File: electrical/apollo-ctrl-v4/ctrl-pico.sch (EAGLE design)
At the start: 30 parts, among them J1 ESP32-PICO-KIT, J2 DNP, J3 DNP, U1 24LC01BT-I/SN

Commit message: Update valve board schematic
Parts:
- added C5, C7: 1u, apollo-ctrl-v4:CAP0805
- added C6: 0.1u, apollo-ctrl-v4:CAP0805
- added C8: 47uF, SparkFun-Capacitors:47UF-POLAR-PANASONIC_D-35V-20%
- added J4: (no value), SparkFun-Connectors:CONN_02
- added J5: M5PWR, SparkFun-Connectors:USB_A_SMT_FEMALE
- added J6: DNP, SparkFun-Connectors:CONN_03
- added JP1, JP2, JP3: M5PWR, SparkFun-Jumpers:JUMPER-SMT_2_NO_NO-SILK
- added R20, R21: 100, apollo-ctrl-v4:RESISTOR0805-RES
- added U2: M5STACK, apollo-ctrl-v4:M5STACK
- C4: value 0.1u -> DNP
- R2, R3, R4: value 10K -> DNP
- U1: value 24LC01BT-I/SN -> DNP (24LC01)
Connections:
- removed net GPIO18: J1.IO18, U$1.PIN15
- removed net GPIO19: J1.IO19, U$1.PIN42
- removed net GPIO21: J1.IO21, U$1.PIN18
- new net !IRQ!: J1.IO21, U$1.PIN16
- new net M33V: C5.1, C6.1, U2.3V3
- new net M5V: JP1.2, U2.5V
- new net MRX: R21.2, U2.G3-RXD1
- new net MRX2: J6.1, U2.G13-RXD2
- new net MSCL: JP2.2, U2.G33-SCL
- new net MSDA: JP3.2, U2.G32-SDA
- new net MTX: R20.2, U2.G1-TXD1
- new net MTX2: J6.3, U2.G14-TXD2
- new net SCL2: J1.IO19
- new net SDA2: J1.IO18
- net +5V: now also C7.1, C8.+, J4.2, J5.VBUS, JP1.1
- net GND: now also C5.2, C6.2, C7.2, C8.-, J4.1, J5.GND, J5.SHLD, J6.2, U2.GND
- net GPIO22: now also R20.1, U$1.PIN15; no longer U$1.PIN17
- net GPIO23: now also R21.1, U$1.PIN42; no longer U$1.PIN16
- net SCL: now also JP2.1
- net SDA: now also JP3.1
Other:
- note added: "DigiKey: WM6294CT-ND"
- note added: "M5 hole: 3.1mm, 44mm C2C Pads 4.6mm (rows) 2.54mm (cols), 1.66mm x 2.6mm"
- note added: "NO PERIPHERAL USE For I2C on board M5Stack"

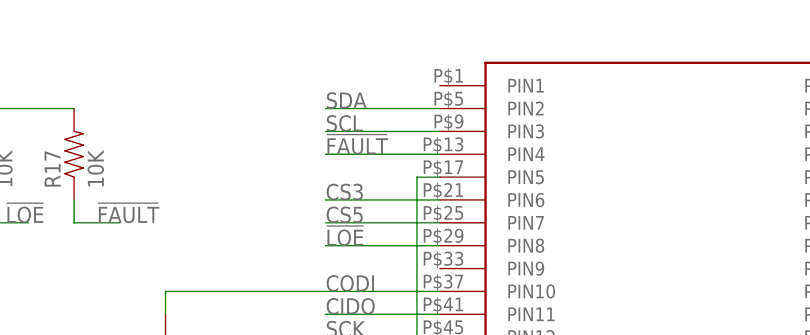
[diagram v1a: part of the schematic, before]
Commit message: Add stepper drivers to the valve board schematic. No guarantee that they fit, but if they do not another board can be made.
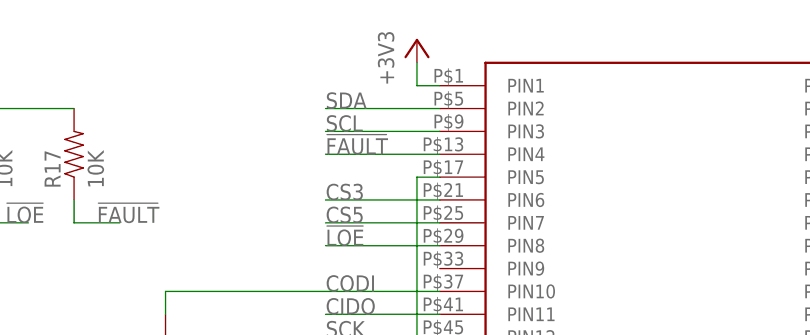
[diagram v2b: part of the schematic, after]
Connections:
- net +3V3: now also U$1.PIN1
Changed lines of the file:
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@@
 <part name="J6" library="SparkFun-Connectors" deviceset="CONN_03" device="" value="DNP"/>
 <part name="GND16" library="supply1" deviceset="GND" device=""/>
+<part name="+3V5" library="supply1" deviceset="+3V3" device=""/>
 </parts>
 <sheets>
@@
 <instance part="GND16" gate="1" x="289.56" y="96.52" smashed="yes">
 <attribute name="VALUE" x="287.02" y="93.98" size="1.778" layer="96"/>
+</instance>
+<instance part="+3V5" gate="G$1" x="104.14" y="182.88" smashed="yes">
+<attribute name="VALUE" x="101.6" y="177.8" size="1.778" layer="96" rot="R90"/>
 </instance>
 </instances>
@@
 <junction x="55.88" y="175.26"/>
 </segment>
-</net>
+<segment>
+<pinref part="+3V5" gate="G$1" pin="+3V3"/>
+<wire x1="104.14" y1="180.34" x2="104.14" y2="177.8" width="0.1524" layer="91"/>
+<pinref part="U$1" gate="G$1" pin="PIN1"/>
+<wire x1="104.14" y1="177.8" x2="106.68" y2="177.8" width="0.1524" layer="91"/>
+</segment>
+</net>

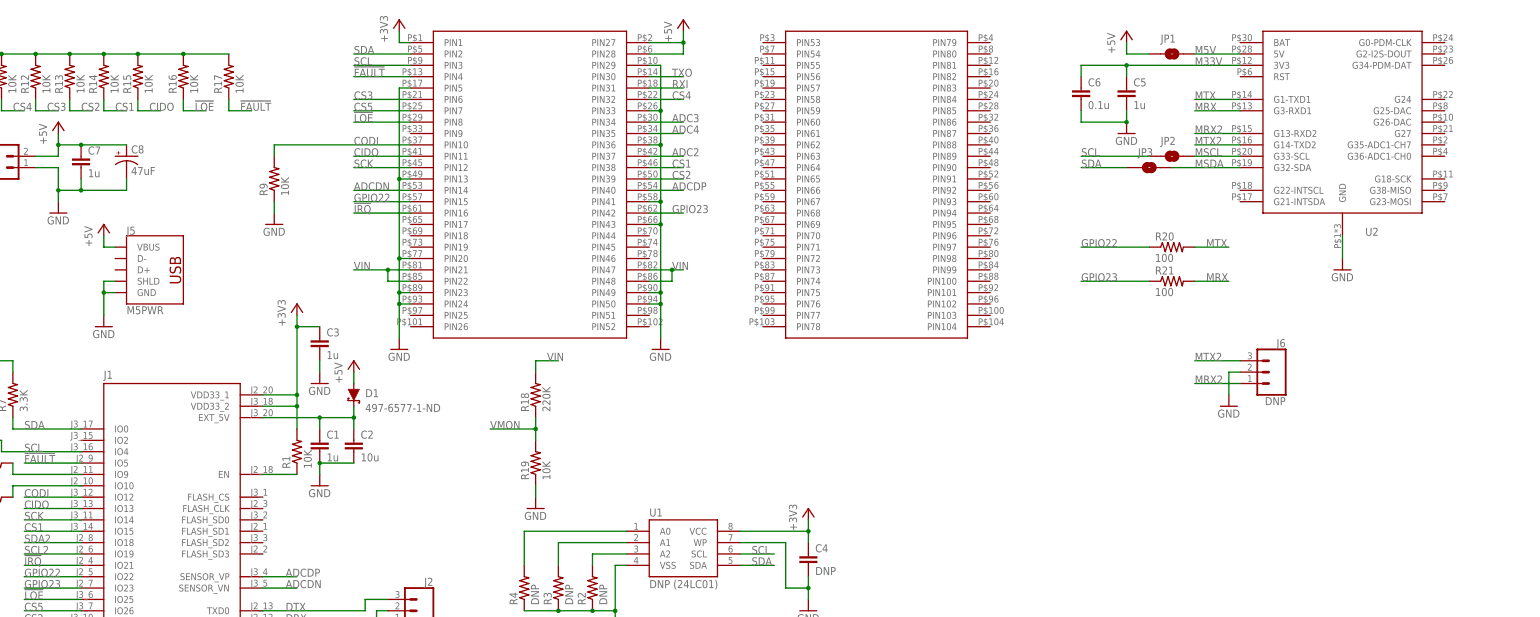
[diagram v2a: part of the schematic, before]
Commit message: Switch Apollo control board to use discrete SPI LCD and no M5-Stack
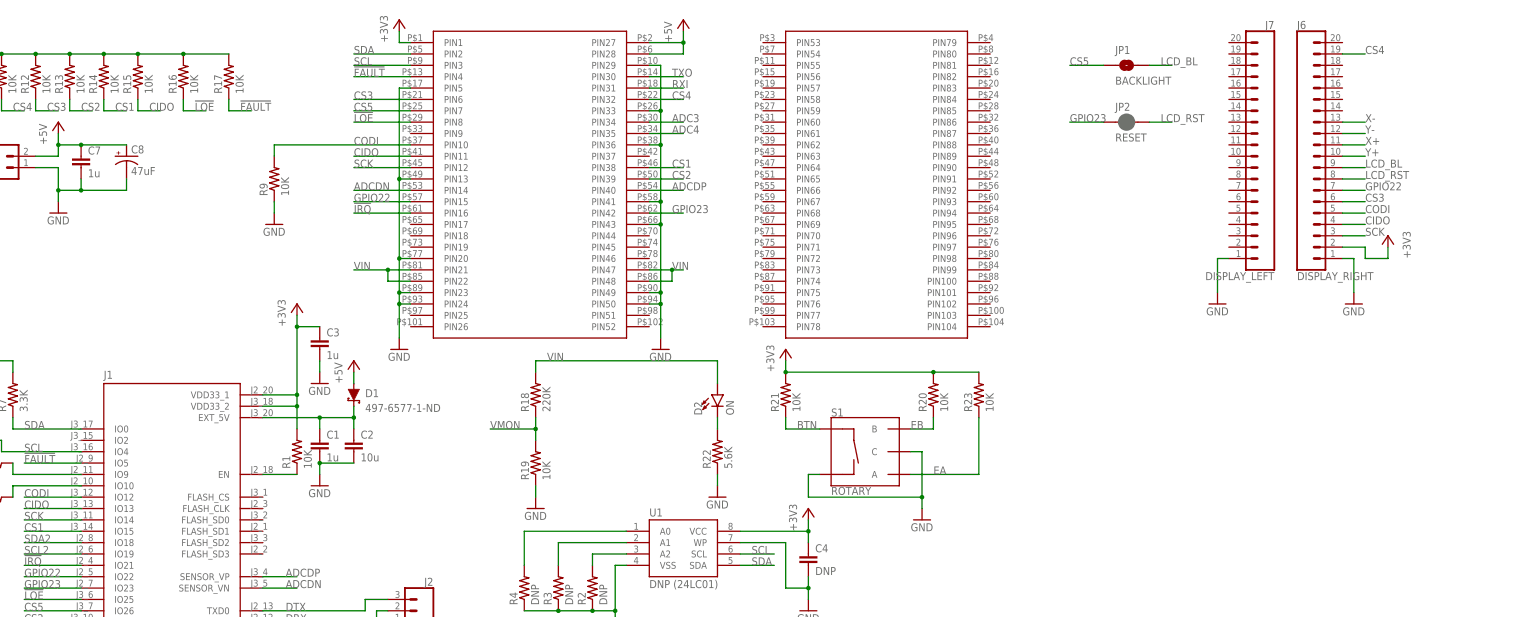
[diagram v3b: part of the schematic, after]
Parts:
- removed C5: 1u, apollo-ctrl-v4:CAP0805
- removed C6: 0.1u, apollo-ctrl-v4:CAP0805
- removed J5: M5PWR, SparkFun-Connectors:USB_A_SMT_FEMALE
- removed JP3: M5PWR, SparkFun-Jumpers:JUMPER-SMT_2_NO_NO-SILK
- removed U2: M5STACK, apollo-ctrl-v4:M5STACK
- added D2: ON, SparkFun-LED:LED-GREEN0603
- added J7: DISPLAY_LEFT, SparkFun-Connectors:CONN_20
- added R22: 5.6K, apollo-ctrl-v4:RESISTOR0805-RES
- added R23: 10K, apollo-ctrl-v4:RESISTOR0805-RES
- added S1: ROTARY, SparkFun-Switches:ENCODER-SWITCH
- J6: value DNP -> DISPLAY_RIGHT; device SparkFun-Connectors:CONN_03 -> SparkFun-Connectors:CONN_20
- JP1: value M5PWR -> BACKLIGHT
- JP2: value M5PWR -> RESET; device SparkFun-Jumpers:JUMPER-SMT_2_NO_NO-SILK -> SparkFun-Jumpers:JUMPER-SMT_2_NC_PASTE_NO-SILK
- R20, R21: value 100 -> 10K
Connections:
- removed net M33V: C5.1, C6.1, U2.3V3
- removed net M5V: JP1.2, U2.5V
- removed net MRX: R21.2, U2.G3-RXD1
- removed net MRX2: J6.1, U2.G13-RXD2
- removed net MSCL: JP2.2, U2.G33-SCL
- removed net MSDA: JP3.2, U2.G32-SDA
- removed net MTX: R20.2, U2.G1-TXD1
- removed net MTX2: J6.3, U2.G14-TXD2
- new net BTN: R21.1, S1.SW+
- new net EA: R23.1, S1.A
- new net EB: R20.1, S1.B
- new net LCD_BL: J6.9, JP1.2
- new net LCD_RST: J6.8, JP2.2
- new net VLED: D2.C, R22.2
- new net X+: J6.11
- new net X-: J6.13
- new net Y+: J6.10
- new net Y-: J6.12
- net +3V3: now also J6.2, R20.2, R21.2, R23.2
- net +5V: no longer J5.VBUS, JP1.1
- net ADC2: no longer U$1.PIN37
- net CIDO: now also J6.4
- net CODI: now also J6.5
- net CS3: now also J6.6
- net CS4: now also J6.19
- net CS5: now also JP1.1
- net GND: now also J6.1, J7.1, R22.1, S1.C, S1.SW-; no longer C5.2, C6.2, J5.GND, J5.SHLD, J6.2, U2.GND
- net GPIO22: now also J6.7; no longer R20.1
- net GPIO23: now also JP2.1; no longer R21.1
- net SCK: now also J6.3
- net SCL: no longer JP2.1
- net SDA: no longer JP3.1
- net VIN: now also D2.A
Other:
- note removed: "DigiKey: WM6294CT-ND"
- note removed: "M5 hole: 3.1mm, 44mm C2C Pads 4.6mm (rows) 2.54mm (cols), 1.66mm x 2.6mm"
- note removed: "NO PERIPHERAL USE For I2C on board M5Stack"
- moved on the sheet: JP1, R20, R21
